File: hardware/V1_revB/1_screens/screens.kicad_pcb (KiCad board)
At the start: 2 copper layers, 34 x 46.9 mm, 5 parts, among them J1 , J2 1431, J3 4086, J4 326, J5 4383

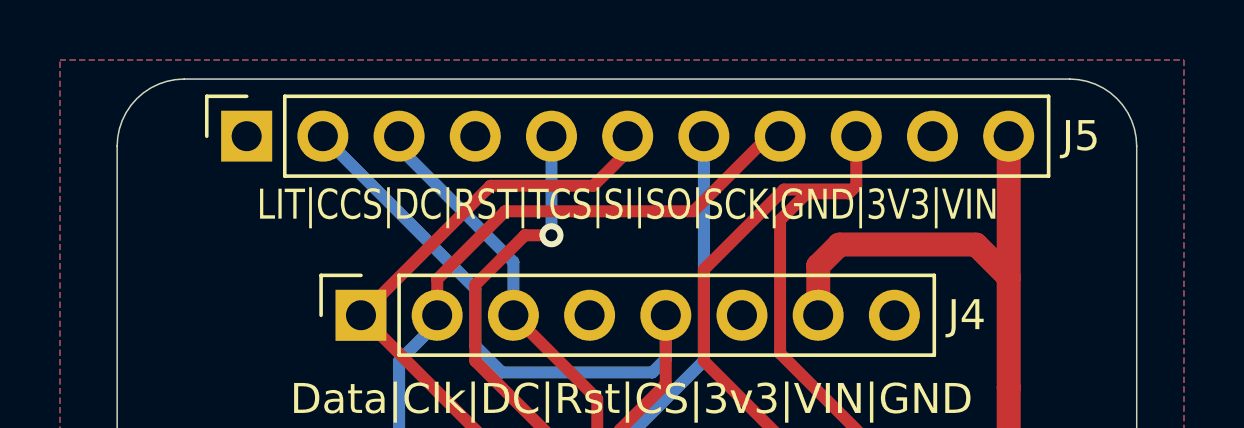
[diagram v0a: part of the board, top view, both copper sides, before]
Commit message: Feat(Hw): UpdateKiCadProjectAndStandardizeComponentProperties
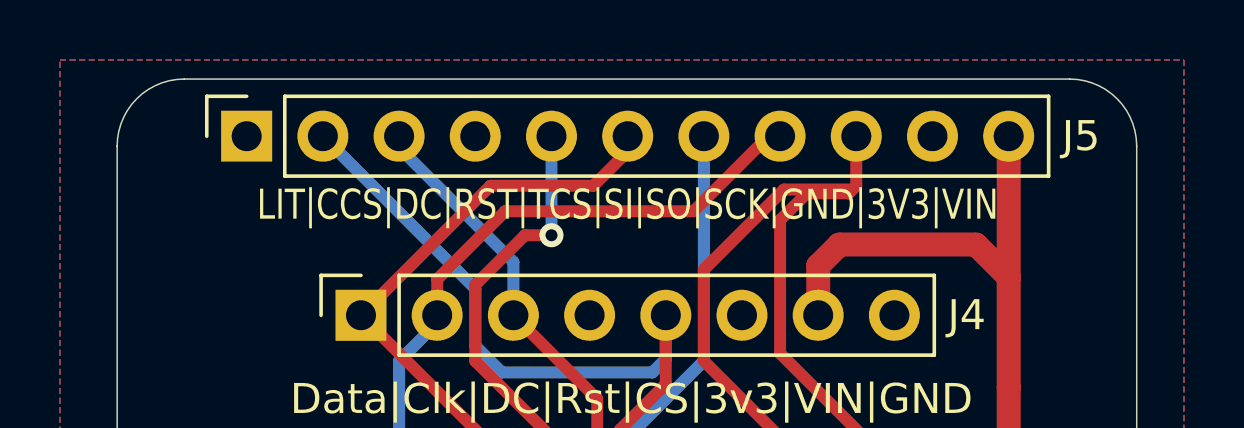
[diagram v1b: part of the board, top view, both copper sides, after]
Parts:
- J1: value (none) -> ~
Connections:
- J1 pad 10: Net-(J1-Pad10) -> unconnected-(J1-Pin_10-Pad10)
- J1 pad 11: Net-(J1-Pad11) -> unconnected-(J1-Pin_11-Pad11)
- J1 pad 12: Net-(J1-Pad12) -> unconnected-(J1-Pin_12-Pad12)
- J1 pad 20: Net-(J1-Pad20) -> unconnected-(J1-Pin_20-Pad20)
- J1 pad 21: Net-(J1-Pad21) -> unconnected-(J1-Pin_21-Pad21)
- J1 pad 22: Net-(J1-Pad22) -> unconnected-(J1-Pin_22-Pad22)
- J1 pad 23: Net-(J1-Pad23) -> unconnected-(J1-Pin_23-Pad23)
- J1 pad 24: Net-(J1-Pad24) -> unconnected-(J1-Pin_24-Pad24)
- J1 pad 25: Net-(J1-Pad25) -> unconnected-(J1-Pin_25-Pad25)
- J1 pad 26: Net-(J1-Pad26) -> unconnected-(J1-Pin_26-Pad26)
- J1 pad 3: Net-(J1-Pad3) -> unconnected-(J1-Pin_3-Pad3)
- J1 pad 5: Net-(J1-Pad5) -> unconnected-(J1-Pin_5-Pad5)
- J1 pad 6: Net-(J1-Pad6) -> unconnected-(J1-Pin_6-Pad6)
- J1 pad 7: Net-(J1-Pad7) -> unconnected-(J1-Pin_7-Pad7)
- J1 pad 8: Net-(J1-Pad8) -> unconnected-(J1-Pin_8-Pad8)
- J1 pad 9: Net-(J1-Pad9) -> unconnected-(J1-Pin_9-Pad9)
- J2 pad 4: Net-(J2-Pad4) -> unconnected-(J2-Pin_4-Pad4)
- J2 pad 8: Net-(J2-Pad8) -> unconnected-(J2-Pin_8-Pad8)
- J2 pad 9: Net-(J2-Pad9) -> unconnected-(J2-Pin_9-Pad9)
- J3 pad 11: Net-(J3-Pad11) -> unconnected-(J3-Pin_11-Pad11)
- J3 pad 12: Net-(J3-Pad12) -> unconnected-(J3-Pin_12-Pad12)
- J3 pad 13: Net-(J3-Pad13) -> unconnected-(J3-Pin_13-Pad13)
- J3 pad 2: Net-(J3-Pad2) -> unconnected-(J3-Pin_2-Pad2)
- J4 pad 4: Net-(J4-Pad4) -> unconnected-(J4-Pin_4-Pad4)
- J4 pad 6: Net-(J4-Pad6) -> unconnected-(J4-Pin_6-Pad6)
- J5 pad 1: Net-(J5-Pad1) -> unconnected-(J5-Pin_1-Pad1)
- J5 pad 10: Net-(J5-Pad10) -> unconnected-(J5-Pin_10-Pad10)
- J5 pad 4: Net-(J5-Pad4) -> unconnected-(J5-Pin_4-Pad4)
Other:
- outline, holes or cut-outs redrawn
- net class 3V removed
- net class 5V removed
- net class Default removed
